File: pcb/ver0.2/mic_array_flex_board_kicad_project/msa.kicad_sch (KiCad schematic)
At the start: 24 parts, among them U2 MP23DB01HPTR, U5 MP23DB01HPTR, U6 MP23DB01HPTR, U7 MP23DB01HPTR

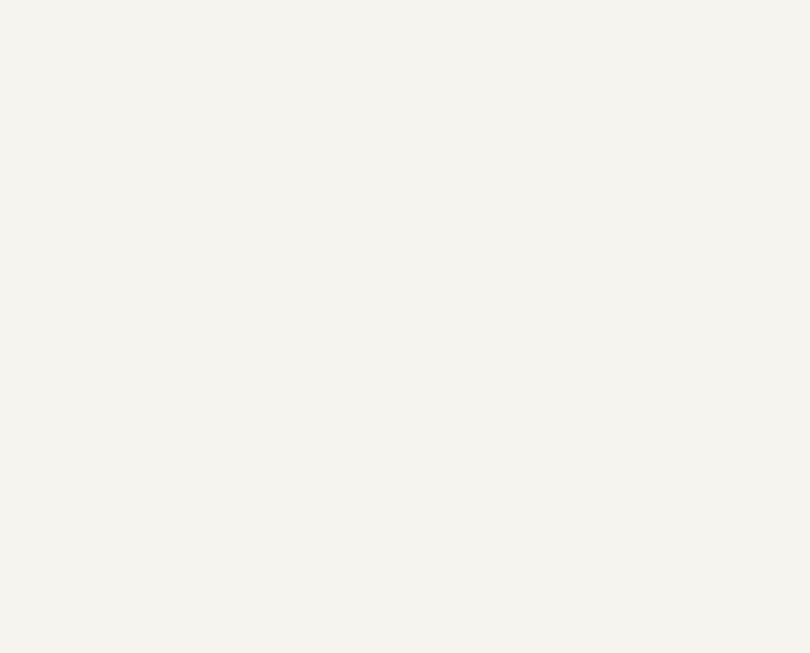
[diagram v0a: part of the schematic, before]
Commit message: make slim stack connector PLUG footprint + symbol, add slim stack connector to flex pcb
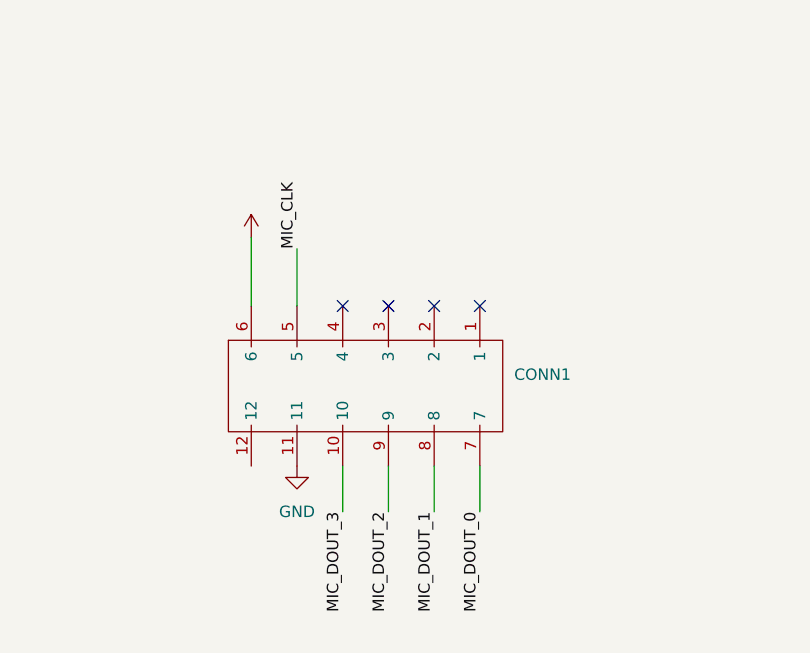
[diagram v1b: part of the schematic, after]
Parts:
- added CONN1: (no value), OpenSourceSmartGlasses:slim_stack_molex_PLUG_5035521222, symbol MSA_lib:slim_stack_12pos_5035521222_schematic
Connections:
- net +3V3: now also CONN1.6
- net GND: now also CONN1.11
- net MIC_CLK: now also CONN1.5
- net MIC_DOUT_0: now also CONN1.7
- net MIC_DOUT_1: now also CONN1.8
- net MIC_DOUT_2: now also CONN1.9
- net MIC_DOUT_3: now also CONN1.10
- no-connect marks 0 -> 4
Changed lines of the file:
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@@
   (junction (at 215.9 53.34) (diameter 0) (color 0 0 0 0)
   )
+  (no_connect (at 106.68 105.41))
+  (no_connect (at 121.92 105.41))
+  (no_connect (at 116.84 105.41))
+  (no_connect (at 111.76 105.41))
   (wire (pts (xy 26.67 43.18) (xy 26.67 40.64))
     (stroke (width 0) (type default) (color 0 0 0 0))
@@
     (stroke (width 0) (type default) (color 0 0 0 0))
   )
+  (wire (pts (xy 121.92 123.19) (xy 121.92 128.27))
+    (stroke (width 0) (type default) (color 0 0 0 0))
+  )
   (wire (pts (xy 195.58 39.37) (xy 203.2 39.37))
     (stroke (width 0) (type default) (color 0 0 0 0))
@@
     (stroke (width 0) (type default) (color 0 0 0 0))
   )
+  (wire (pts (xy 96.52 97.79) (xy 96.52 105.41))
+    (stroke (width 0) (type default) (color 0 0 0 0))
+  )
   (wire (pts (xy 187.96 34.29) (xy 190.5 34.29))
     (stroke (width 0) (type default) (color 0 0 0 0))
@@
     (stroke (width 0) (type default) (color 0 0 0 0))
   )
+  (wire (pts (xy 116.84 123.19) (xy 116.84 128.27))
+    (stroke (width 0) (type default) (color 0 0 0 0))
+  )
   (wire (pts (xy 77.47 43.18) (xy 77.47 40.64))
     (stroke (width 0) (type default) (color 0 0 0 0))
@@
     (stroke (width 0) (type default) (color 0 0 0 0))
   )
+  (wire (pts (xy 111.76 123.19) (xy 111.76 128.27))
+    (stroke (width 0) (type default) (color 0 0 0 0))
+  )
   (wire (pts (xy 101.6 39.37) (xy 101.6 34.29))
     (stroke (width 0) (type default) (color 0 0 0 0))
@@
     (stroke (width 0) (type default) (color 0 0 0 0))
   )
+  (wire (pts (xy 106.68 123.19) (xy 106.68 128.27))
+    (stroke (width 0) (type default) (color 0 0 0 0))
+  )
   (wire (pts (xy 165.1 53.34) (xy 172.72 53.34))
     (stroke (width 0) (type default) (color 0 0 0 0))
@@
   )
   (wire (pts (xy 40.64 55.88) (xy 30.48 55.88))
+    (stroke (width 0) (type default) (color 0 0 0 0))
+  )
+  (wire (pts (xy 101.6 99.06) (xy 101.6 105.41))
     (stroke (width 0) (type default) (color 0 0 0 0))
   )
@@
     (effects (font (size 1.27 1.27)) (justify left bottom))
   )
+  (label "MIC_DOUT_1" (at 116.84 128.27 270)
+    (effects (font (size 1.27 1.27)) (justify right bottom))
+  )
   (label "MIC_CLK" (at 132.08 55.88 0)
     (effects (font (size 1.27 1.27)) (justify left bottom))
   )
+  (label "MIC_CLK" (at 101.6 99.06 90)
+    (effects (font (size 1.27 1.27)) (justify left bottom))
+  )
+  (label "MIC_DOUT_2" (at 111.76 128.27 270)
+    (effects (font (size 1.27 1.27)) (justify right bottom))
+  )
   (label "MIC_DOUT_0" (at 71.12 53.34 180)
     (effects (font (size 1.27 1.27)) (justify right bottom))
@@
     (effects (font (size 1.27 1.27)) (justify left bottom))
   )
+  (label "MIC_DOUT_0" (at 121.92 128.27 270)
+    (effects (font (size 1.27 1.27)) (justify right bottom))
+  )
   (label "MIC_DOUT_2" (at 172.72 53.34 180)
+    (effects (font (size 1.27 1.27)) (justify right bottom))
+  )
+  (label "MIC_DOUT_3" (at 106.68 128.27 270)
     (effects (font (size 1.27 1.27)) (justify right bottom))
   )
@@
     (pin "2")
   )
+  (symbol (lib_id "MSA_lib:slim_stack_12pos_5035521222_schematic") (at 102.87 111.76 0) (unit 1)
+    (in_bom yes) (on_board yes) (fields_autoplaced)
+    (property "Reference" "CONN1" (id 0) (at 125.73 113.0299 0)
+      (effects (font (size 1.27 1.27)) (justify left))
+    )
+    (property "Value" "" (id 1) (at 125.73 115.5699 0)
+      (effects (font (size 1.27 1.27)) (justify left))
+    )
+    (property "Footprint" "OpenSourceSmartGlasses:slim_stack_molex_PLUG_5035521222" (id 2) (at 104.14 96.52 0)
+      (effects (font (size 1.27 1.27)) hide)
+    )
+    (property "Datasheet" "" (id 3) (at 93.98 109.22 0)
+      (effects (font (size 1.27 1.27)) hide)
+    )
+    (pin "1")
+    (pin "10")
+    (pin "11")
+    (pin "12")
+    (pin "2")
+    (pin "3")
+    (pin "4")
+    (pin "5")
+    (pin "6")
+    (pin "7")
+    (pin "8")
+    (pin "9")
+  )
+  (symbol (lib_name "+3V3_1") (lib_id "power:+3V3") (at 96.52 97.79 0) (unit 1)
+    (in_bom yes) (on_board yes) (fields_autoplaced)
+    (property "Reference" "#PWR0101" (id 0) (at 96.52 101.6 0)
+      (effects (font (size 1.27 1.27)) hide)
+    )
+    (property "Value" "" (id 1) (at 96.52 92.71 0))
+    (property "Footprint" "" (id 2) (at 96.52 97.79 0)
+      (effects (font (size 1.27 1.27)) hide)
+    )
+    (property "Datasheet" "" (id 3) (at 96.52 97.79 0)
+      (effects (font (size 1.27 1.27)) hide)
+    )
+    (pin "1")
+  )
+  (symbol (lib_name "GND_1") (lib_id "power:GND") (at 101.6 123.19 0) (unit 1)
+    (in_bom yes) (on_board yes) (fields_autoplaced)
+    (property "Reference" "#PWR0102" (id 0) (at 101.6 129.54 0)
+      (effects (font (size 1.27 1.27)) hide)
+    )
+    (property "Value" "GND" (id 1) (at 101.6 128.27 0))
+    (property "Footprint" "" (id 2) (at 101.6 123.19 0)
+      (effects (font (size 1.27 1.27)) hide)
+    )
+    (property "Datasheet" "" (id 3) (at 101.6 123.19 0)
+      (effects (font (size 1.27 1.27)) hide)
+    )
+    (pin "1")
+  )
   (sheet_instances
     (path "/" (page "1"))
@@
       (reference "#PWR046") (unit 1) (value "GND") (footprint "")
     )
+    (path "/78498ecb-11cf-4bf1-a520-ea447553fdca"
+      (reference "#PWR0101") (unit 1) (value "+3V3") (footprint "")
+    )
+    (path "/e137d15c-250c-4d9c-b0a0-d220301c596f"
+      (reference "#PWR0102") (unit 1) (value "GND") (footprint "")
+    )
     (path "/00000000-0000-0000-0000-0000620966e9"
       (reference "C2") (unit 1) (value "0.1uF") (footprint "Capacitor_SMD:C_0402_1005Metric")
@@
       (reference "C25") (unit 1) (value "1uF") (footprint "Capacitor_SMD:C_0402_1005Metric")
     )
+    (path "/3bd9005a-a6d1-4101-bcdd-7e4abb068227"
+      (reference "CONN1") (unit 1) (value "slim_stack_12pos_5035521222_schematic") (footprint "OpenSourceSmartGlasses:slim_stack_molex_PLUG_5035521222")
+    )
     (path "/00000000-0000-0000-0000-0000620966ca"

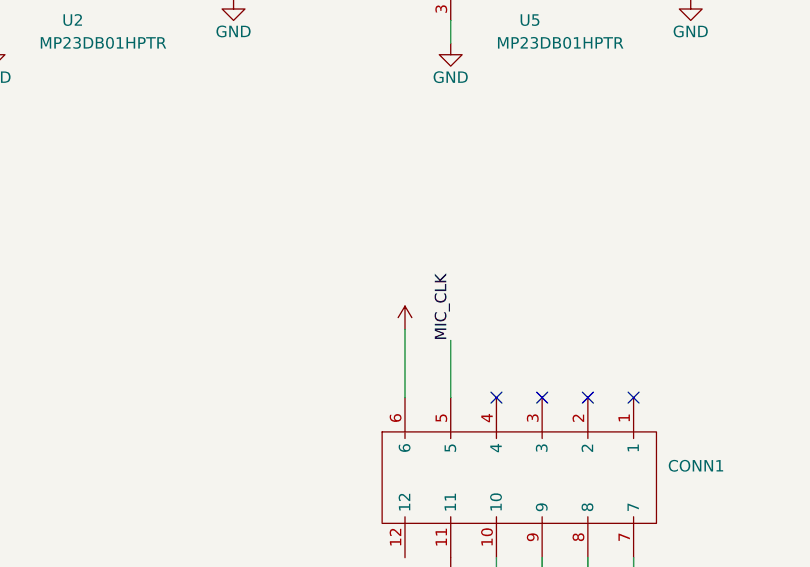
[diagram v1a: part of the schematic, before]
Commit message: add slimstack receptacle to library, add to main rigid board
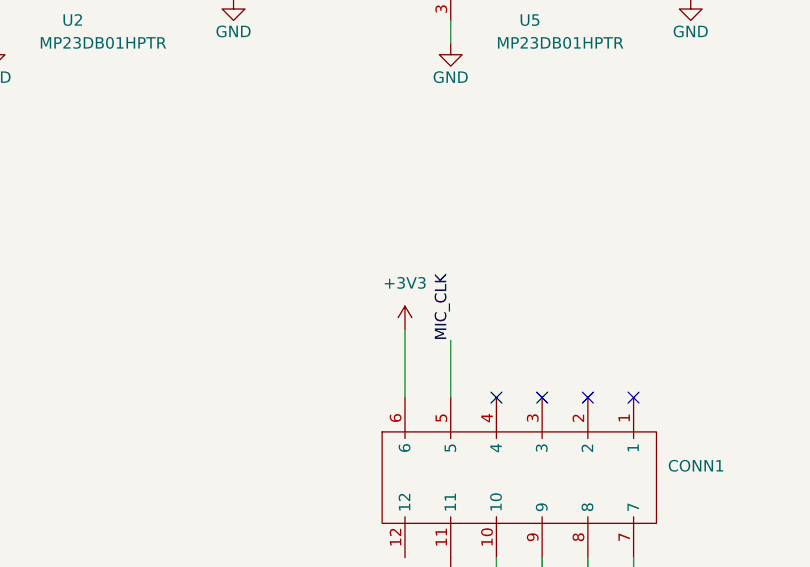
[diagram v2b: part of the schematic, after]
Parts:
- CONN1: footprint OpenSourceSmartGlasses:slim_stack_molex_PLUG_5035521222 -> (none)
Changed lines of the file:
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@@
       (effects (font (size 1.27 1.27)) (justify left))
     )
-    (property "Footprint" "OpenSourceSmartGlasses:slim_stack_molex_PLUG_5035521222" (id 2) (at 104.14 96.52 0)
+    (property "Footprint" "" (id 2) (at 104.14 96.52 0)
       (effects (font (size 1.27 1.27)) hide)
     )
@@
       (effects (font (size 1.27 1.27)) hide)
     )
-    (property "Value" "" (id 1) (at 96.52 92.71 0))
+    (property "Value" "+3V3" (id 1) (at 96.52 92.71 0))
     (property "Footprint" "" (id 2) (at 96.52 97.79 0)
       (effects (font (size 1.27 1.27)) hide)
